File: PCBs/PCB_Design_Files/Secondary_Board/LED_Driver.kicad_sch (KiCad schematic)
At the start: 0 parts

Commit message: add driver components
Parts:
- added LED1: SFH 7018A, Project Footprints:SFH_7018A_LEDs, symbol Project_Symbols:SFH_7018A
- added Q5, Q7: 2N7002, Project Footprints:2N7002, symbol Project_Symbols:2N7002
- added Q6, Q8: BSS84, Project Footprints:BSS84, symbol Project_Symbols:BSS84
- added U8: OPA333AIDCKR, Project Footprints:OPA333, symbol Project_Symbols:OPA333AIDCKR

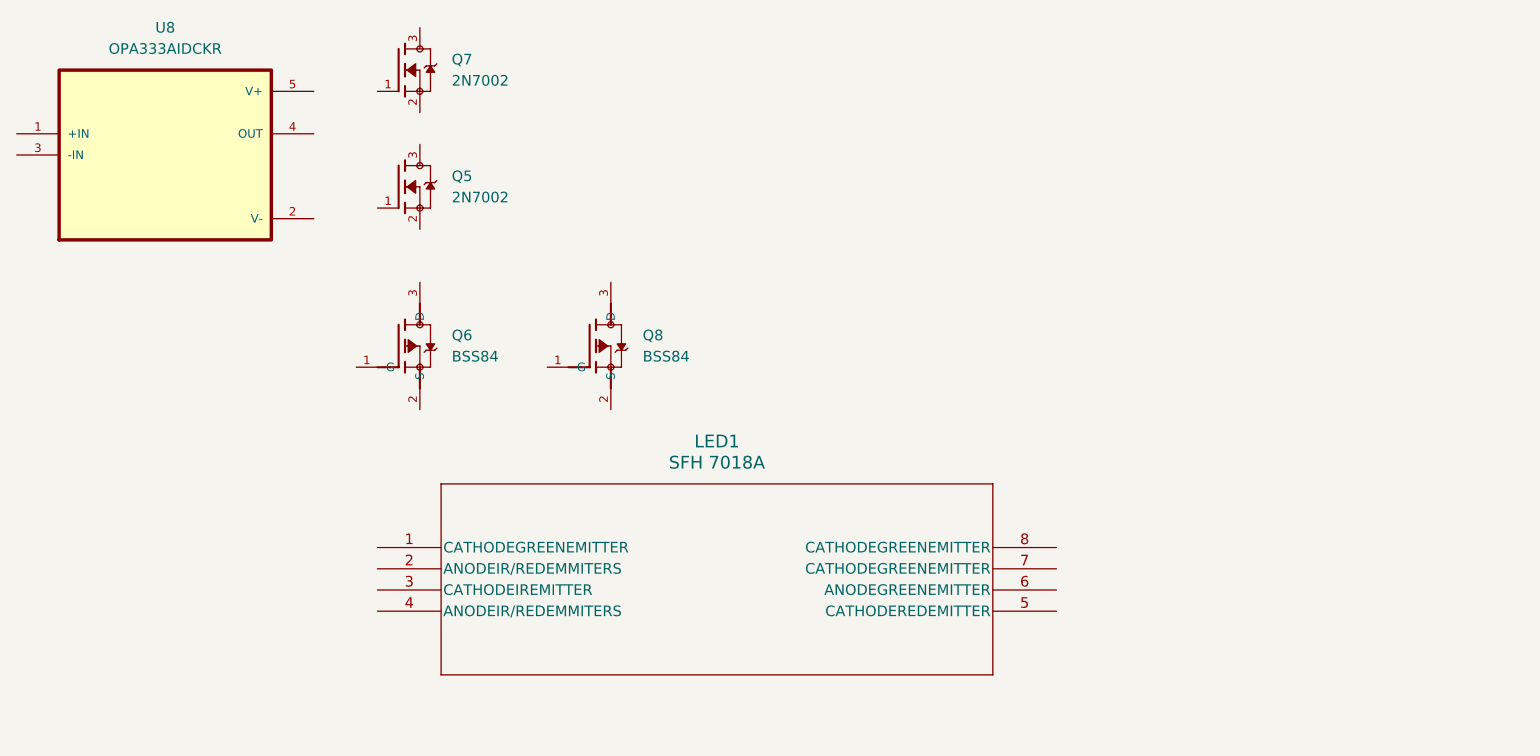
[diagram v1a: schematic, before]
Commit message: LED Driver Schematic
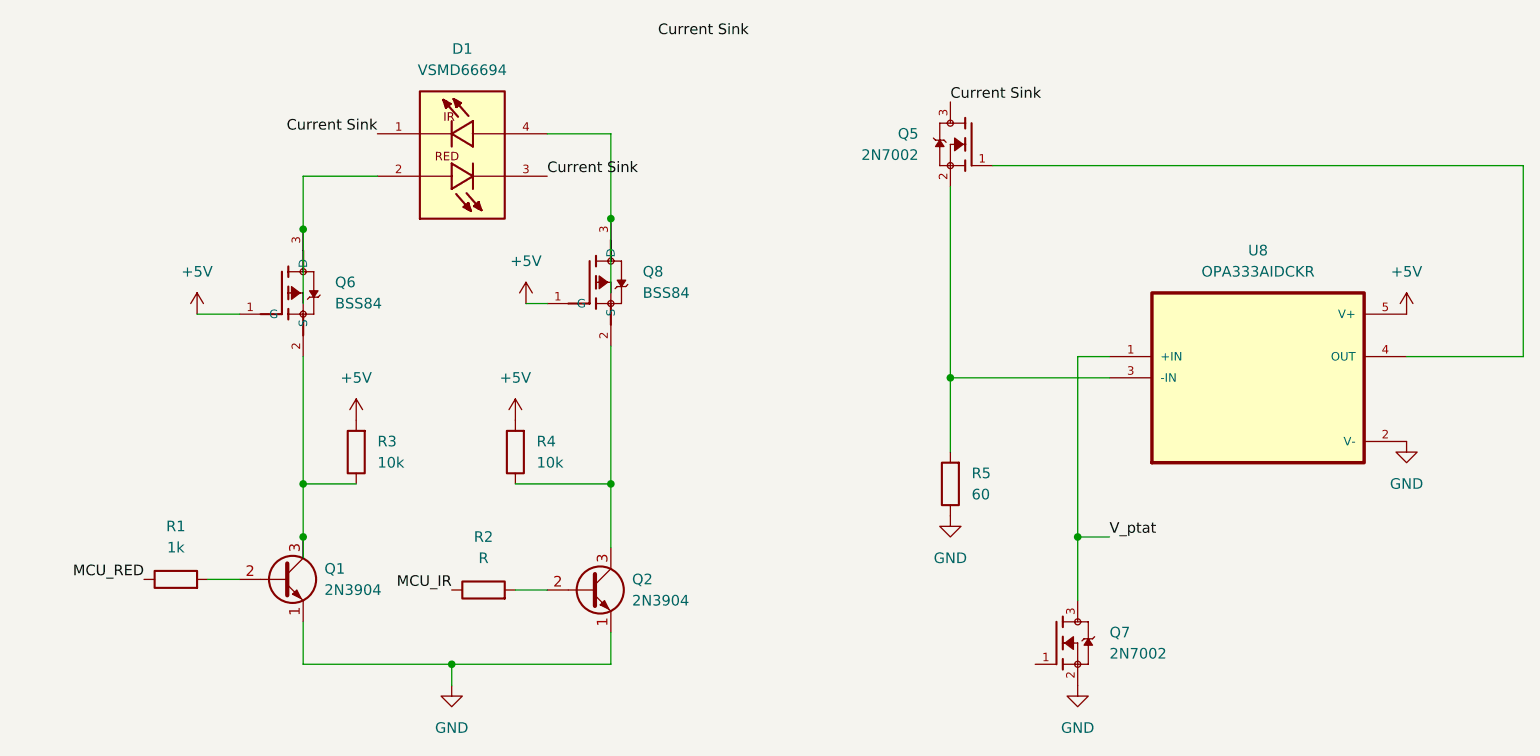
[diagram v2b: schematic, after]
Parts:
- removed LED1: SFH 7018A, Project Footprints:SFH_7018A_LEDs, symbol Project_Symbols:SFH_7018A
- added D1: VSMD66694, Project Footprints:DIO_VSMD66694, symbol Project_Symbols:VSMD66694
- added Q1, Q2: 2N3904, Package_TO_SOT_THT:TO-92_Inline, symbol Transistor_BJT:2N3904
- added R1: 1k, symbol Device:R
- added R2: R, symbol Device:R
- added R3, R4: 10k, symbol Device:R
- added R5: 60, symbol Device:R
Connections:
- net +5V: now reaches Q6.1 (G)
- net +5V: now also Q8.1 (G), U8.5 (V+), R3.2, R4.2
- net at Q6.2 (S): now also Q1.3 (C), R3.1
- net at Q6.3 (D): now also D1.2
- net at Q5.1: now also U8.4 (OUT)
- net at Q5.2: now also U8.3 (-IN), R5.2
- net Current Sink: now reaches Q5.3
- net Current Sink: now also D1.1, D1.3
- net at Q8.2 (S): now also Q2.3 (C), R4.1
- net at Q8.3 (D): now also D1.4
- net V_ptat: now reaches U8.1 (+IN)
- net V_ptat: now also Q7.3
- net GND: now reaches U8.2 (V-)
- net GND: now also Q7.2, Q1.1 (E), Q2.1 (E), R5.1
- new net: Q1.2 (B), R1.2
- new net: Q2.2 (B), R2.2
- new net MCU_IR: R2.1
- new net MCU_RED: R1.1
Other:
- moved on the sheet: Q5, Q6, Q7, Q8, U8

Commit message: LED Driver added to PCB
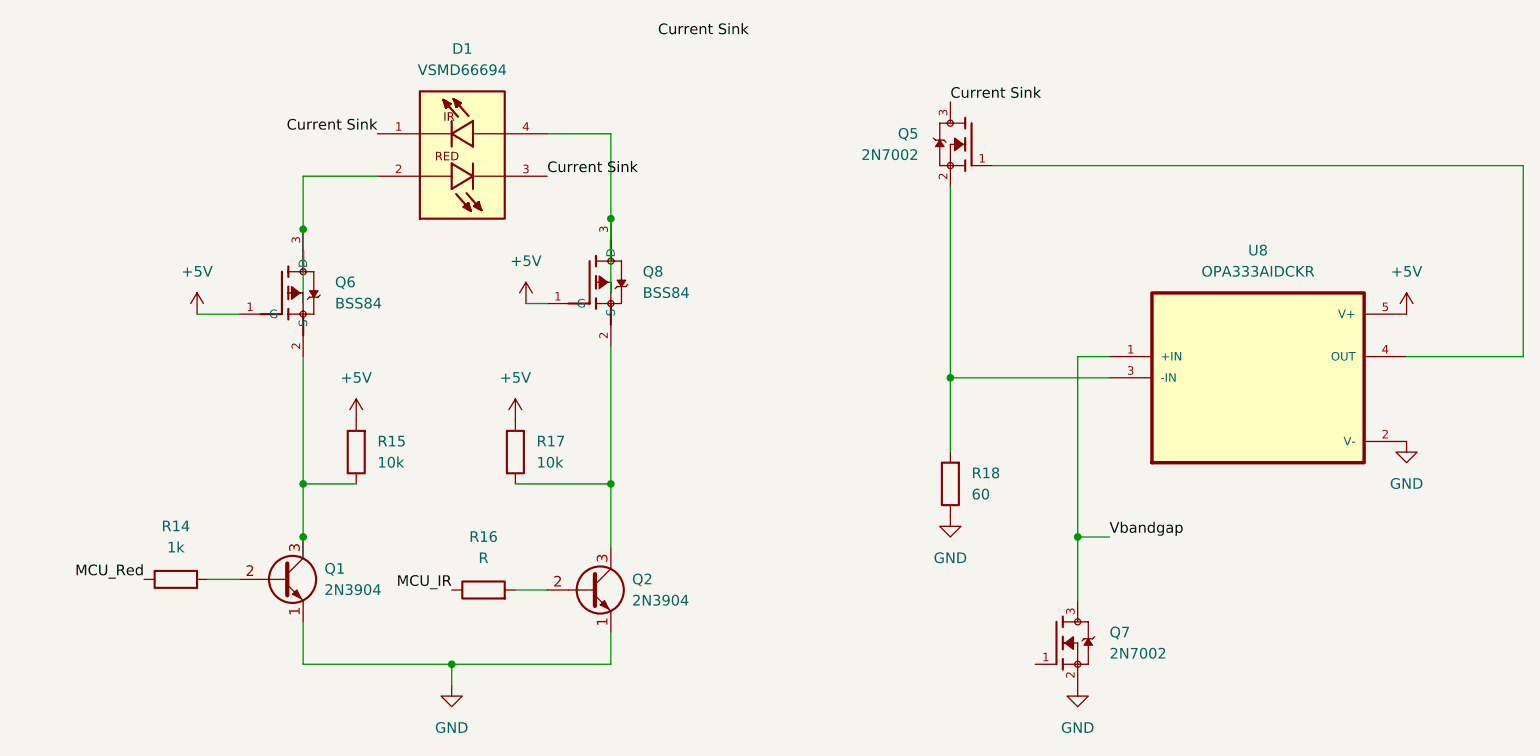
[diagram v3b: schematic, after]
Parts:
- renumbered R1 to R14, R3 to R15, R2 to R16, R4 to R17, R5 to R18
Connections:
- net MCU_RED renamed MCU_Red
- net V_ptat renamed Vbandgap
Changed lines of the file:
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@@
 		)
 	)
-	(label "MCU_RED"
+	(label "MCU_Red"
 		(at 80.01 127 180)
 		(effects
@@
 		)
 	)
-	(label "V_ptat"
+	(label "Vbandgap"
 		(at 195.58 121.92 0)
 		(effects
@@
 		(on_board yes)
 		(dnp no)
-		(property "Reference" "#PWR05"
+		(property "Reference" "#PWR0111"
 			(at 105.41 111.76 0)
 			(effects
@@
 		)
 		(instances
+			(project "Secondary_Board"
+				(path "/2f5986e4-77b2-4f5d-ab91-80ba6228eb8b/16ecf950-1853-427b-9137-65792483b2a5"
+					(reference "#PWR0111")
+					(unit 1)
+				)
+			)
 			(project "LED_Driver"
 				(path "/ed36e940-b5c2-4fa7-8175-f729e6b712de"
@@
 		(dnp no)
 		(fields_autoplaced yes)
-		(property "Reference" "#PWR02"
+		(property "Reference" "#PWR0113"
 			(at 116.84 146.05 0)
 			(effects
@@
 		)
 		(instances
+			(project "Secondary_Board"
+				(path "/2f5986e4-77b2-4f5d-ab91-80ba6228eb8b/16ecf950-1853-427b-9137-65792483b2a5"
+					(reference "#PWR0113")
+					(unit 1)
+				)
+			)
 			(project ""
 				(path "/ed36e940-b5c2-4fa7-8175-f729e6b712de"
@@
 		(dnp no)
 		(fields_autoplaced yes)
-		(property "Reference" "#PWR09"
+		(property "Reference" "#PWR0116"
 			(at 176.53 125.73 0)
 			(effects
@@
 		)
 		(instances
+			(project "Secondary_Board"
+				(path "/2f5986e4-77b2-4f5d-ab91-80ba6228eb8b/16ecf950-1853-427b-9137-65792483b2a5"
+					(reference "#PWR0116")
+					(unit 1)
+				)
+			)
 			(project "LED_Driver"
 				(path "/ed36e940-b5c2-4fa7-8175-f729e6b712de"
@@
 		)
 		(instances
+			(project "Secondary_Board"
+				(path "/2f5986e4-77b2-4f5d-ab91-80ba6228eb8b/16ecf950-1853-427b-9137-65792483b2a5"
+					(reference "Q1")
+					(unit 1)
+				)
+			)
 			(project ""
 				(path "/ed36e940-b5c2-4fa7-8175-f729e6b712de"
@@
 		(dnp no)
 		(fields_autoplaced yes)
-		(property "Reference" "R5"
+		(property "Reference" "R18"
 			(at 179.07 114.2999 0)
 			(effects
@@
 		)
 		(instances
+			(project "Secondary_Board"
+				(path "/2f5986e4-77b2-4f5d-ab91-80ba6228eb8b/16ecf950-1853-427b-9137-65792483b2a5"
+					(reference "R18")
+					(unit 1)
+				)
+			)
 			(project "LED_Driver"
 				(path "/ed36e940-b5c2-4fa7-8175-f729e6b712de"
@@
 		(dnp no)
 		(fields_autoplaced yes)
-		(property "Reference" "R2"
+		(property "Reference" "R16"
 			(at 120.65 121.92 90)
 			(effects
@@
 		)
 		(instances
+			(project "Secondary_Board"
+				(path "/2f5986e4-77b2-4f5d-ab91-80ba6228eb8b/16ecf950-1853-427b-9137-65792483b2a5"
+					(reference "R16")
+					(unit 1)
+				)
+			)
 			(project ""
 				(path "/ed36e940-b5c2-4fa7-8175-f729e6b712de"
@@
 		(dnp no)
 		(fields_autoplaced yes)
-		(property "Reference" "#PWR06"
+		(property "Reference" "#PWR0114"
 			(at 124.46 111.76 0)
 			(effects
@@
 		)
 		(instances
+			(project "Secondary_Board"
+				(path "/2f5986e4-77b2-4f5d-ab91-80ba6228eb8b/16ecf950-1853-427b-9137-65792483b2a5"
+					(reference "#PWR0114")
+					(unit 1)
+				)
+			)
 			(project "LED_Driver"
 				(path "/ed36e940-b5c2-4fa7-8175-f729e6b712de"
@@
 		(dnp no)
 		(fields_autoplaced yes)
-		(property "Reference" "#PWR07"
+		(property "Reference" "#PWR0118"
 			(at 231.14 99.06 0)
 			(effects
@@
 		)
 		(instances
+			(project "Secondary_Board"
+				(path "/2f5986e4-77b2-4f5d-ab91-80ba6228eb8b/16ecf950-1853-427b-9137-65792483b2a5"
+					(reference "#PWR0118")
+					(unit 1)
+				)
+			)
 			(project "LED_Driver"
 				(path "/ed36e940-b5c2-4fa7-8175-f729e6b712de"
@@
 		(on_board yes)
 		(dnp no)
-		(property "Reference" "Q?"
+		(property "Reference" "Q6"
 			(at 102.87 91.4399 0)
 			(effects
@@
 			(project "LED_Driver"
 				(path "/ed36e940-b5c2-4fa7-8175-f729e6b712de"
-					(reference "Q?")
+					(reference "Q3")
 					(unit 1)
 				)
@@
 		(dnp no)
 		(fields_autoplaced yes)
-		(property "Reference" "R4"
+		(property "Reference" "R17"
 			(at 127 110.4899 0)
 			(effects
@@
 		)
 		(instances
+			(project "Secondary_Board"
+				(path "/2f5986e4-77b2-4f5d-ab91-80ba6228eb8b/16ecf950-1853-427b-9137-65792483b2a5"
+					(reference "R17")
+					(unit 1)
+				)
+			)
 			(project "LED_Driver"
 				(path "/ed36e940-b5c2-4fa7-8175-f729e6b712de"
@@
 		)
 		(instances
+			(project "Secondary_Board"
+				(path "/2f5986e4-77b2-4f5d-ab91-80ba6228eb8b/16ecf950-1853-427b-9137-65792483b2a5"
+					(reference "Q2")
+					(unit 1)
+				)
+			)
 			(project ""
 				(path "/ed36e940-b5c2-4fa7-8175-f729e6b712de"
@@
 		(on_board yes)
 		(dnp no)
-		(property "Reference" "Q?"
+		(property "Reference" "Q5"
 			(at 172.72 73.6599 0)
 			(effects
@@
 			(project "LED_Driver"
 				(path "/ed36e940-b5c2-4fa7-8175-f729e6b712de"
-					(reference "Q?")
+					(reference "Q5")
 					(unit 1)
 				)
@@
 		(dnp no)
 		(fields_autoplaced yes)
-		(property "Reference" "R1"
+		(property "Reference" "R14"
 			(at 83.82 120.65 90)
 			(effects
@@
 		)
 		(instances
+			(project "Secondary_Board"
+				(path "/2f5986e4-77b2-4f5d-ab91-80ba6228eb8b/16ecf950-1853-427b-9137-65792483b2a5"
+					(reference "R14")
+					(unit 1)
+				)
+			)
 			(project ""
 				(path "/ed36e940-b5c2-4fa7-8175-f729e6b712de"
@@
 		(dnp no)
 		(fields_autoplaced yes)
-		(property "Reference" "#PWR01"
+		(property "Reference" "#PWR0112"
 			(at 86.36 99.06 0)
 			(effects
@@
 		)
 		(instances
+			(project "Secondary_Board"
+				(path "/2f5986e4-77b2-4f5d-ab91-80ba6228eb8b/16ecf950-1853-427b-9137-65792483b2a5"
+					(reference "#PWR0112")
+					(unit 1)
+				)
+			)
 			(project ""
 				(path "/ed36e940-b5c2-4fa7-8175-f729e6b712de"
@@
 		(dnp no)
 		(fields_autoplaced yes)
-		(property "Reference" "Q?"
+		(property "Reference" "Q8"
 			(at 139.7 90.1699 0)
 			(effects
@@
 			(project "LED_Driver"
 				(path "/ed36e940-b5c2-4fa7-8175-f729e6b712de"
-					(reference "Q?")
+					(reference "Q4")
 					(unit 1)
 				)
@@
 		(dnp no)
 		(fields_autoplaced yes)
-		(property "Reference" "U?"
+		(property "Reference" "U8"
 			(at 213.36 87.63 0)
 			(effects
@@
 			(project "LED_Driver"
 				(path "/ed36e940-b5c2-4fa7-8175-f729e6b712de"
-					(reference "U?")
+					(reference "U1")
 					(unit 1)
 				)
@@
 		)
 		(instances
+			(project "Secondary_Board"
+				(path "/2f5986e4-77b2-4f5d-ab91-80ba6228eb8b/16ecf950-1853-427b-9137-65792483b2a5"
+					(reference "D1")
+					(unit 1)
+				)
+			)
 			(project ""
 				(path "/ed36e940-b5c2-4fa7-8175-f729e6b712de"
@@
 		(dnp no)
 		(fields_autoplaced yes)
-		(property "Reference" "R3"
+		(property "Reference" "R15"
 			(at 107.95 110.4899 0)
 			(effects
@@
 		)
 		(instances
+			(project "Secondary_Board"
+				(path "/2f5986e4-77b2-4f5d-ab91-80ba6228eb8b/16ecf950-1853-427b-9137-65792483b2a5"
+					(reference "R15")
+					(unit 1)
+				)
+			)
 			(project ""
 				(path "/ed36e940-b5c2-4fa7-8175-f729e6b712de"
@@
 		(dnp no)
 		(fields_autoplaced yes)
-		(property "Reference" "Q?"
+		(property "Reference" "Q7"
 			(at 195.58 133.3499 0)
 			(effects
@@
 			(project "LED_Driver"
 				(path "/ed36e940-b5c2-4fa7-8175-f729e6b712de"
-					(reference "Q?")
+					(reference "Q6")
 					(unit 1)
 				)
@@
 		(dnp no)
 		(fields_autoplaced yes)
-		(property "Reference" "#PWR08"
+		(property "Reference" "#PWR0117"
 			(at 191.77 146.05 0)
 			(effects
@@
 		)
 		(instances
+			(project "Secondary_Board"
+				(path "/2f5986e4-77b2-4f5d-ab91-80ba6228eb8b/16ecf950-1853-427b-9137-65792483b2a5"
+					(reference "#PWR0117")
+					(unit 1)
+				)
+			)
 			(project "LED_Driver"
 				(path "/ed36e940-b5c2-4fa7-8175-f729e6b712de"
@@
 		(dnp no)
 		(fields_autoplaced yes)
-		(property "Reference" "#PWR04"
+		(property "Reference" "#PWR0115"
 			(at 125.73 97.79 0)
 			(effects
@@
 		)
 		(instances
+			(project "Secondary_Board"
+				(path "/2f5986e4-77b2-4f5d-ab91-80ba6228eb8b/16ecf950-1853-427b-9137-65792483b2a5"
+					(reference "#PWR0115")
+					(unit 1)
+				)
+			)
 			(project "LED_Driver"
 				(path "/ed36e940-b5c2-4fa7-8175-f729e6b712de"
@@
 		(dnp no)
 		(fields_autoplaced yes)
-		(property "Reference" "#PWR03"
+		(property "Reference" "#PWR0119"
 			(at 231.14 116.84 0)
 			(effects
@@
 		)
 		(instances
+			(project "Secondary_Board"
+				(path "/2f5986e4-77b2-4f5d-ab91-80ba6228eb8b/16ecf950-1853-427b-9137-65792483b2a5"
+					(reference "#PWR0119")
+					(unit 1)
+				)
+			)
 			(project "LED_Driver"
 				(path "/ed36e940-b5c2-4fa7-8175-f729e6b712de"

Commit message: LED Driver Updates
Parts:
- added R19: 1k, Resistor_SMD:R_0603_1608Metric_Pad0.98x0.95mm_HandSolder, symbol Device:R
- R14, R15, R16, R17, R18: footprint (none) -> Resistor_SMD:R_0603_1608Metric_Pad0.98x0.95mm_HandSolder
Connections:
- net at Q7.1: now also R19.1
- new net MCU_OPA_CTRL: R19.2
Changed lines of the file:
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@@
+	(wire
+		(pts
+			(xy 180.34 137.16) (xy 186.69 137.16)
+		)
+		(stroke
+			(width 0)
+			(type default)
+		)
+	)
 	(wire
 		(pts
@@
 			(width 0)
 			(type default)
-		)
-	)
-	(label "MCU_IR"
-		(at 116.84 128.27 180)
-		(effects
-			(font
-				(size 1.27 1.27)
-			)
-			(justify right bottom)
 		)
 	)
@@
 		)
 	)
-	(label "MCU_Red"
-		(at 80.01 127 180)
-		(effects
-			(font
-				(size 1.27 1.27)
-			)
-			(justify right bottom)
-		)
-	)
 	(label "Current Sink"
 		(at 152.4 62.23 180)
@@
 		)
 	)
-	(label "Vbandgap"
-		(at 195.58 121.92 0)
+	(global_label "MCU_IR"
+		(shape input)
+		(at 116.84 128.27 180)
+		(fields_autoplaced yes)
 		(effects
 			(font
 				(size 1.27 1.27)
 			)
-			(justify left bottom)
+			(justify right)
+		)
+		(property "Intersheetrefs" "${INTERSHEET_REFS}"
+			(at 106.9605 128.27 0)
+			(effects
+				(font
+					(size 1.27 1.27)
+				)
+				(justify right)
+				(hide yes)
+			)
+		)
+	)
+	(global_label "MCU_Red"
+		(shape input)
+		(at 80.01 127 180)
+		(fields_autoplaced yes)
+		(effects
+			(font
+				(size 1.27 1.27)
+			)
+			(justify right)
+		)
+		(property "Intersheetrefs" "${INTERSHEET_REFS}"
+			(at 68.4977 127 0)
+			(effects
+				(font
+					(size 1.27 1.27)
+				)
+				(justify right)
+				(hide yes)
+			)
+		)
+	)
+	(global_label "MCU_OPA_CTRL"
+		(shape input)
+		(at 172.72 137.16 180)
+		(fields_autoplaced yes)
+		(effects
+			(font
+				(size 1.27 1.27)
+			)
+			(justify right)
+		)
+		(property "Intersheetrefs" "${INTERSHEET_REFS}"
+			(at 155.5229 137.16 0)
+			(effects
+				(font
+					(size 1.27 1.27)
+				)
+				(justify right)
+				(hide yes)
+			)
+		)
+	)
+	(global_label "Vbandgap"
+		(shape input)
+		(at 195.58 121.92 0)
+		(fields_autoplaced yes)
+		(effects
+			(font
+				(size 1.27 1.27)
+			)
+			(justify left)
+		)
+		(property "Intersheetrefs" "${INTERSHEET_REFS}"
+			(at 207.6968 121.92 0)
+			(effects
+				(font
+					(size 1.27 1.27)
+				)
+				(justify left)
+				(hide yes)
+			)
 		)
 	)
@@
 	)
 	(symbol
+		(lib_id "Device:R")
+		(at 176.53 137.16 270)
+		(unit 1)
+		(exclude_from_sim no)
+		(in_bom yes)
+		(on_board yes)
+		(dnp no)
+		(fields_autoplaced yes)
+		(property "Reference" "R19"
+			(at 176.53 130.81 90)
+			(effects
+				(font
+					(size 1.27 1.27)
+				)
+			)
+		)
+		(property "Value" "1k"
+			(at 176.53 133.35 90)
+			(effects
+				(font
+					(size 1.27 1.27)
+				)
+			)
+		)
+		(property "Footprint" "Resistor_SMD:R_0603_1608Metric_Pad0.98x0.95mm_HandSolder"
+			(at 176.53 135.382 90)
+			(effects
+				(font
+					(size 1.27 1.27)
+				)
+				(hide yes)
+			)
+		)
+		(property "Datasheet" "~"
+			(at 176.53 137.16 0)
+			(effects
+				(font
+					(size 1.27 1.27)
+				)
+				(hide yes)
+			)
+		)
+		(property "Description" "Resistor"
+			(at 176.53 137.16 0)
+			(effects
+				(font
+					(size 1.27 1.27)
+				)
+				(hide yes)
+			)
+		)
+		(pin "2"
+		)
+		(pin "1"
+		)
+		(instances
+			(project "Secondary_Board"
+				(path "/2f5986e4-77b2-4f5d-ab91-80ba6228eb8b/16ecf950-1853-427b-9137-65792483b2a5"
+					(reference "R19")
+					(unit 1)
+				)
+			)
+		)
+	)
+	(symbol
 		(lib_id "power:GND")
 		(at 176.53 119.38 0)
@@
 			)
 		)
-		(property "Footprint" ""
+		(property "Footprint" "Resistor_SMD:R_0603_1608Metric_Pad0.98x0.95mm_HandSolder"
 			(at 178.308 115.57 90)
 			(effects
@@
 			)
 		)
-		(property "Footprint" ""
+		(property "Footprint" "Resistor_SMD:R_0603_1608Metric_Pad0.98x0.95mm_HandSolder"
 			(at 120.65 130.048 90)
 			(effects
@@
 			)
 		)
-		(property "Footprint" ""
+		(property "Footprint" "Resistor_SMD:R_0603_1608Metric_Pad0.98x0.95mm_HandSolder"
 			(at 126.238 111.76 90)
 			(effects
@@
 			)
 		)
-		(property "Footprint" ""
+		(property "Footprint" "Resistor_SMD:R_0603_1608Metric_Pad0.98x0.95mm_HandSolder"
 			(at 83.82 128.778 90)
 			(effects
@@
 			)
 		)
-		(property "Footprint" ""
+		(property "Footprint" "Resistor_SMD:R_0603_1608Metric_Pad0.98x0.95mm_HandSolder"
 			(at 107.188 111.76 90)
 			(effects
